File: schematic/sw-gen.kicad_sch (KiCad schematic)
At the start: 4 parts

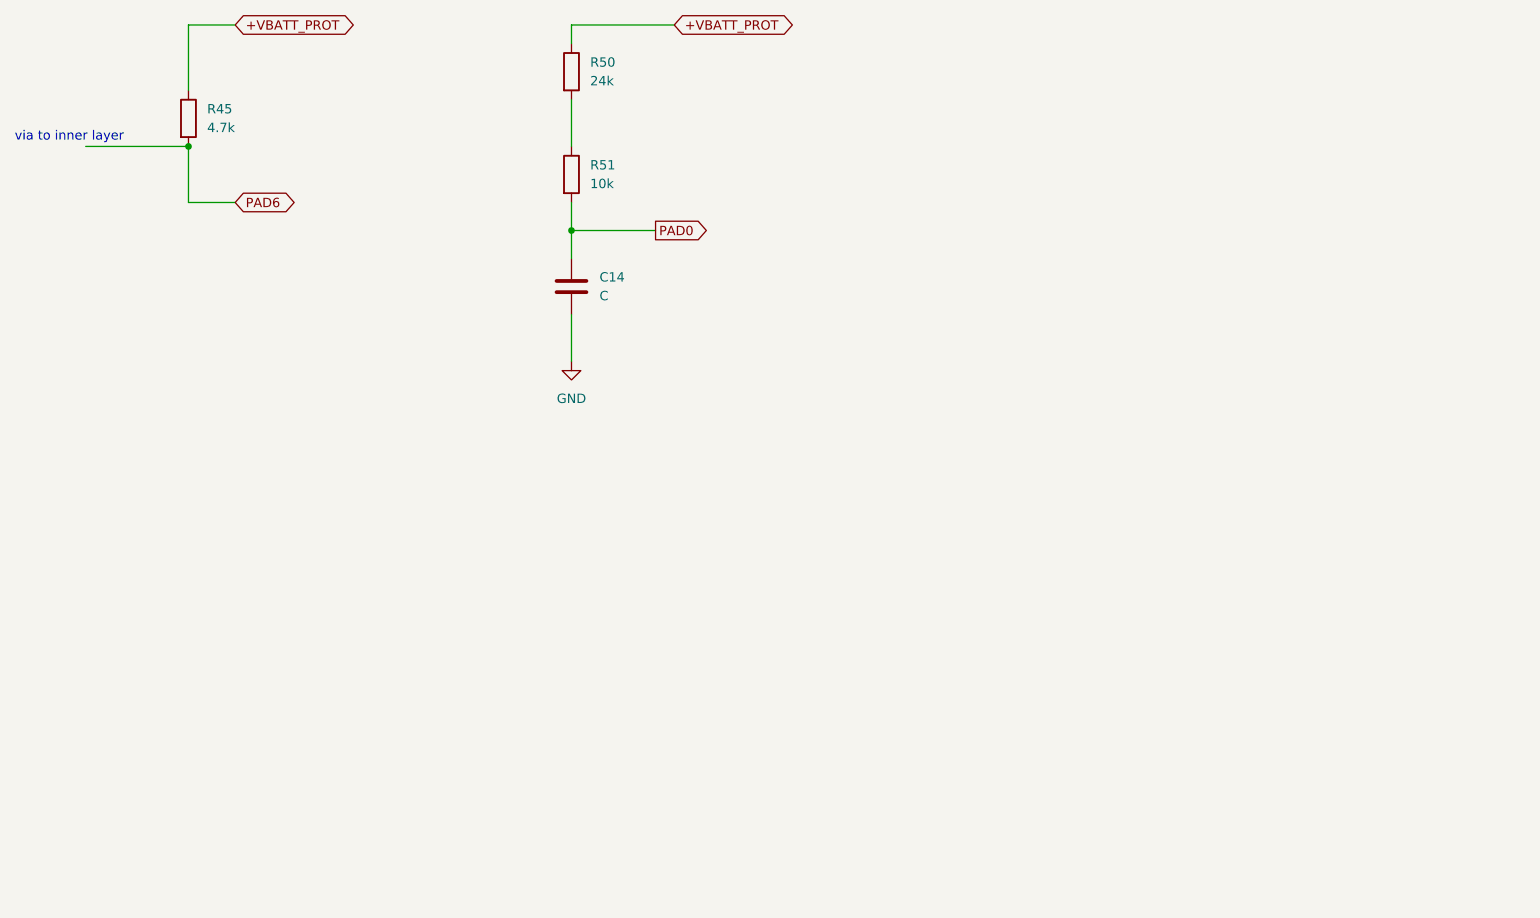
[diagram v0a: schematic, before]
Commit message: Added J5 and assoc. resistor network. Added traceable signals for MYSTERY_SIG
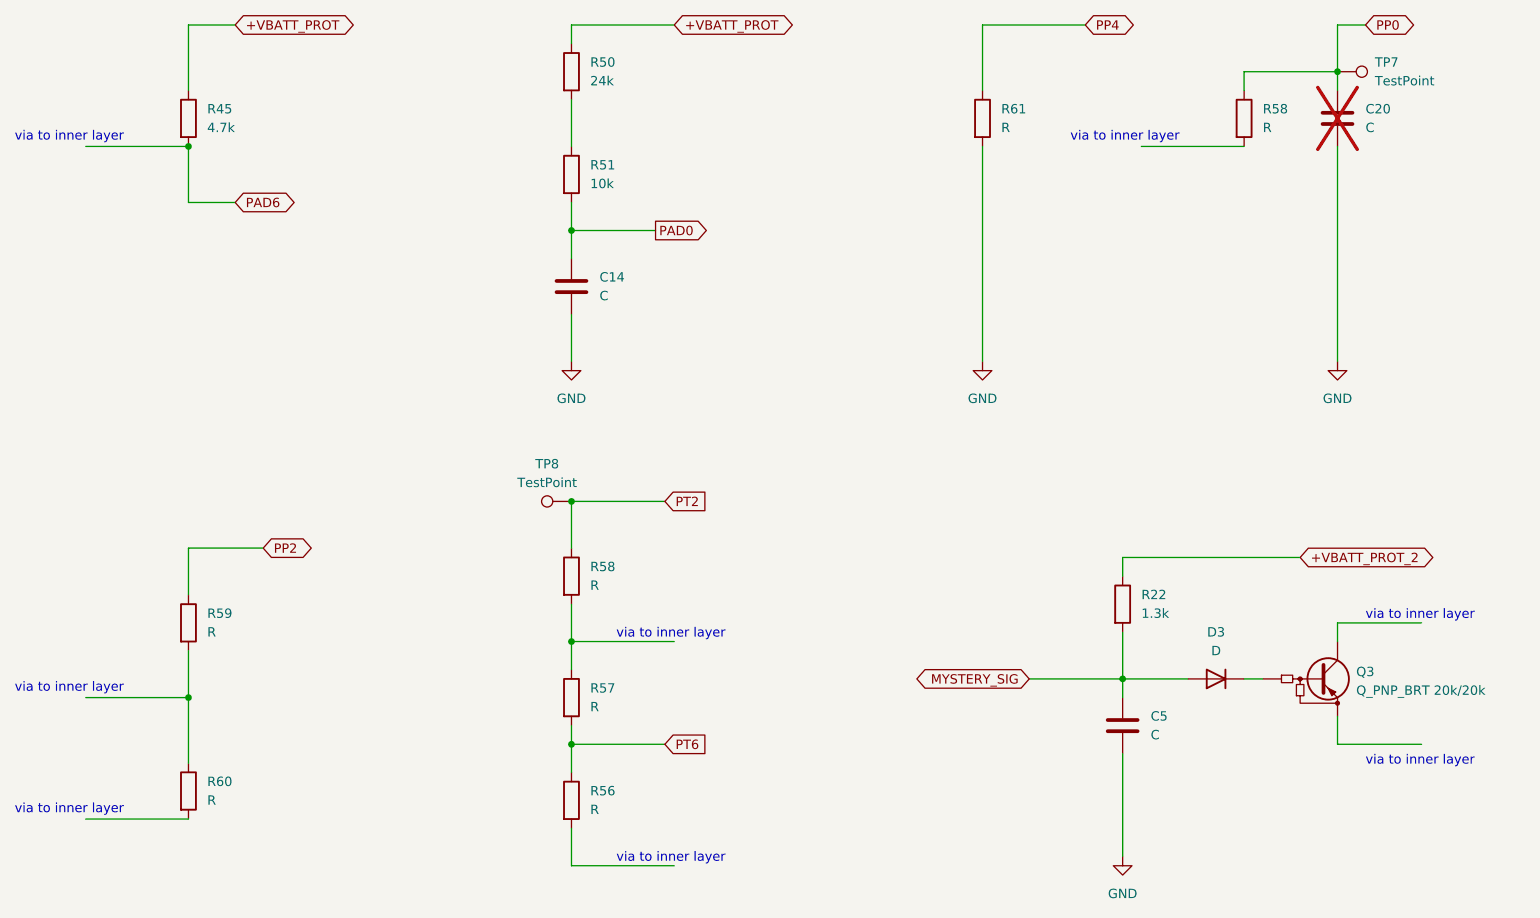
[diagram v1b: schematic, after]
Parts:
- added C20, C5: C, symbol Device:C
- added D3: D, symbol Device:D
- added Q3: Q_PNP_BRT 20k/20k, symbol Device:Q_PNP_BRT
- added R22: 1.3k, symbol Device:R
- added R56, R57, R58 (x2), R59, R60, R61: R, symbol Device:R
- added TP7, TP8: TestPoint, symbol Connector:TestPoint
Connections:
- net GND: now also C20.2, C5.2, R61.2
- new net: R59.2, R60.1
- new net: D3.1 (K), Q3.B
- new net: R57.1, R58.2
- new net +VBATT_PROT_2: R22.1
- new net MYSTERY_SIG: C5.1, D3.2 (A), R22.2
- new net PP0: C20.1, R58.1, TP7.1
- new net PP2: R59.1
- new net PP4: R61.1
- new net PT2: R58.1, TP8.1
- new net PT6: R56.1, R57.2
